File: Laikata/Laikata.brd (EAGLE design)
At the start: 55 x 111 mm, 19 parts, among them IC1_3V3 REG1117, IC2_5V REG1117, U1 S25FL127SABMFI101

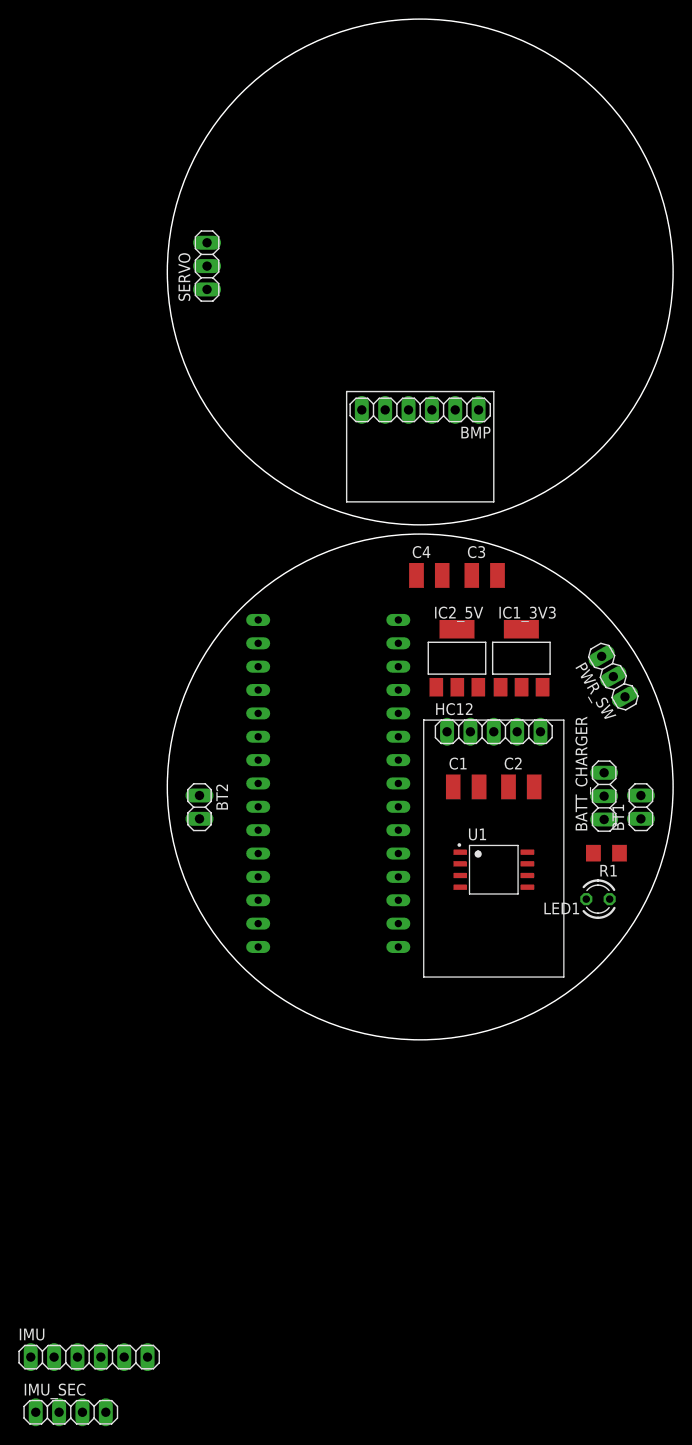
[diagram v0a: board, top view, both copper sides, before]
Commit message: IMU component
Created and added a custom component for the BNO055 sensor
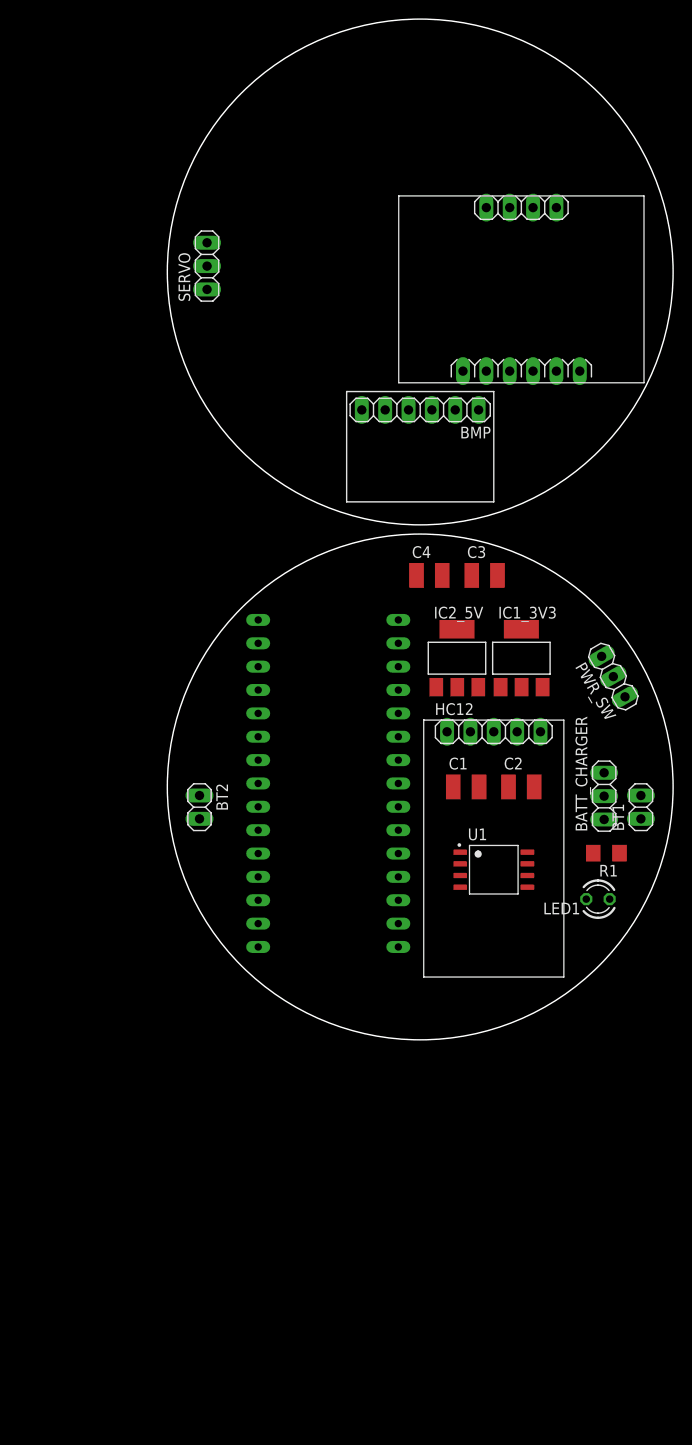
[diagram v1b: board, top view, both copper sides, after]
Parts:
- removed IMU: (no value), pinhead:1X06
- removed IMU_SEC: (no value), pinhead:1X04
- added U$2: IMU, hc12:IMU
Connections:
- net +3V3: now also U$2.VIN; no longer IMU.1
- net GND: now also U$2.GND
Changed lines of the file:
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@@
 <attribute name="VALUE" x="-0.905" y="19.825" size="1.27" layer="27"/>
-</element>
-<element name="IMU" library="pinhead" library_urn="urn:adsk.eagle:library:325" package="1X06" package3d_urn="urn:adsk.eagle:package:22472/2" value="" x="-36" y="-62" smashed="yes">
-<attribute name="NAME" x="-43.6962" y="-60.1712" size="1.27" layer="25" ratio="10"/>
-<attribute name="POPULARITY" value="79" x="-36" y="-62" size="1.778" layer="27" display="off"/>
-<attribute name="VALUE" x="-43.62" y="-65.175" size="1.27" layer="27"/>
-</element>
-<element name="IMU_SEC" library="pinhead" library_urn="urn:adsk.eagle:library:325" package="1X04" package3d_urn="urn:adsk.eagle:package:22407/2" value="" x="-38" y="-68" smashed="yes">
-<attribute name="NAME" x="-43.1562" y="-66.1712" size="1.27" layer="25" ratio="10"/>
-<attribute name="POPULARITY" value="91" x="-38" y="-68" size="1.778" layer="27" display="off"/>
-<attribute name="VALUE" x="-43.08" y="-71.175" size="1.27" layer="27"/>
 </element>
 <element name="HC12" library="hc12" package="HC12" value="" x="8" y="6" smashed="yes">
@@
 <attribute name="VALUE" x="1.65" y="2.825" size="1.27" layer="27"/>
 </element>
+<element name="U$2" library="hc12" package="IMU" value="IMU" x="11" y="63" smashed="yes"/>
 </elements>
 <signals>
@@
 <contactref element="C4" pad="1"/>
 <contactref element="HC12" pad="GND"/>
-<wire x1="5.6" y1="23" x2="-0.4" y2="23" width="0" layer="19" extent="1-1"/>
-<wire x1="-17.62" y1="-14.86" x2="5.6" y2="23" width="0" layer="19" extent="1-1"/>
+<contactref element="U$2" pad="GND"/>
+<wire x1="-17.62" y1="-14.86" x2="9.73" y2="45.22" width="0" layer="19" extent="1-1"/>
 <wire x1="-24" y1="-3.47" x2="-17.62" y2="-14.86" width="0" layer="19" extent="1-1"/>
 <wire x1="-2.38" y1="-9.78" x2="-17.62" y2="-14.86" width="0" layer="19" extent="1-1"/>
@@
 <wire x1="1.7394" y1="10.8504" x2="8.7394" y2="10.8504" width="0" layer="19" extent="1-1"/>
 <wire x1="20" y1="1.54" x2="10.54" y2="6" width="0" layer="19" extent="1-1"/>
+<wire x1="-0.4" y1="23" x2="1.7394" y2="10.8504" width="0" layer="19" extent="1-1"/>
+<wire x1="5.6" y1="23" x2="-0.4" y2="23" width="0" layer="19" extent="1-1"/>
 <wire x1="18.06" y1="-12.2" x2="4.345" y2="-10.905" width="0" layer="19" extent="1-1"/>
-<wire x1="3.81" y1="41" x2="1.7394" y2="10.8504" width="0" layer="19" extent="1-1"/>
+<wire x1="3.81" y1="41" x2="5.6" y2="23" width="0" layer="19" extent="1-1"/>
 <wire x1="-23.18" y1="54.1" x2="3.81" y2="41" width="0" layer="19" extent="1-1"/>
 </signal>
@@
 <contactref element="C2" pad="2"/>
 <contactref element="IC1_3V3" pad="2"/>
-<contactref element="IMU" pad="1"/>
 <contactref element="HC12" pad="VCC"/>
-<wire x1="13.08" y1="6" x2="-42.35" y2="-62" width="0" layer="19" extent="1-1"/>
+<contactref element="U$2" pad="VIN"/>
+<wire x1="11.655" y1="-7.095" x2="4.65" y2="45.22" width="0" layer="19" extent="1-1"/>
+<wire x1="12.4" y1="0" x2="11.655" y2="-7.095" width="0" layer="19" extent="1-1"/>
+<wire x1="13.08" y1="6" x2="12.4" y2="0" width="0" layer="19" extent="1-1"/>
 <wire x1="11.0254" y1="10.8504" x2="13.08" y2="6" width="0" layer="19" extent="1-1"/>
-<wire x1="11.655" y1="-7.095" x2="11.0254" y2="10.8504" width="0" layer="19" extent="1-1"/>
-<wire x1="12.4" y1="0" x2="11.655" y2="-7.095" width="0" layer="19" extent="1-1"/>
-<wire x1="18.828" y1="-7.2" x2="12.4" y2="0" width="0" layer="19" extent="1-1"/>
-<wire x1="6.35" y1="41" x2="18.828" y2="-7.2" width="0" layer="19" extent="1-1"/>
+<wire x1="18.828" y1="-7.2" x2="11.655" y2="-7.095" width="0" layer="19" extent="1-1"/>
+<wire x1="6.35" y1="41" x2="11.0254" y2="10.8504" width="0" layer="19" extent="1-1"/>
 </signal>
 <signal name="N$7">
